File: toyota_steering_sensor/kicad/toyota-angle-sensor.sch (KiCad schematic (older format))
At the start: 32 parts, among them J1 AVR-ISP-6, J2 RJ45, U1 NCP1117-5.0_SOT223, U2 ATMEGA328PB-AU, U3 LS7366R, U4 MCP2515-xSO, U5 AS5047P, U6 TJA1050, Y1 16MHz, Y2 40MHz, Y3 8MHz

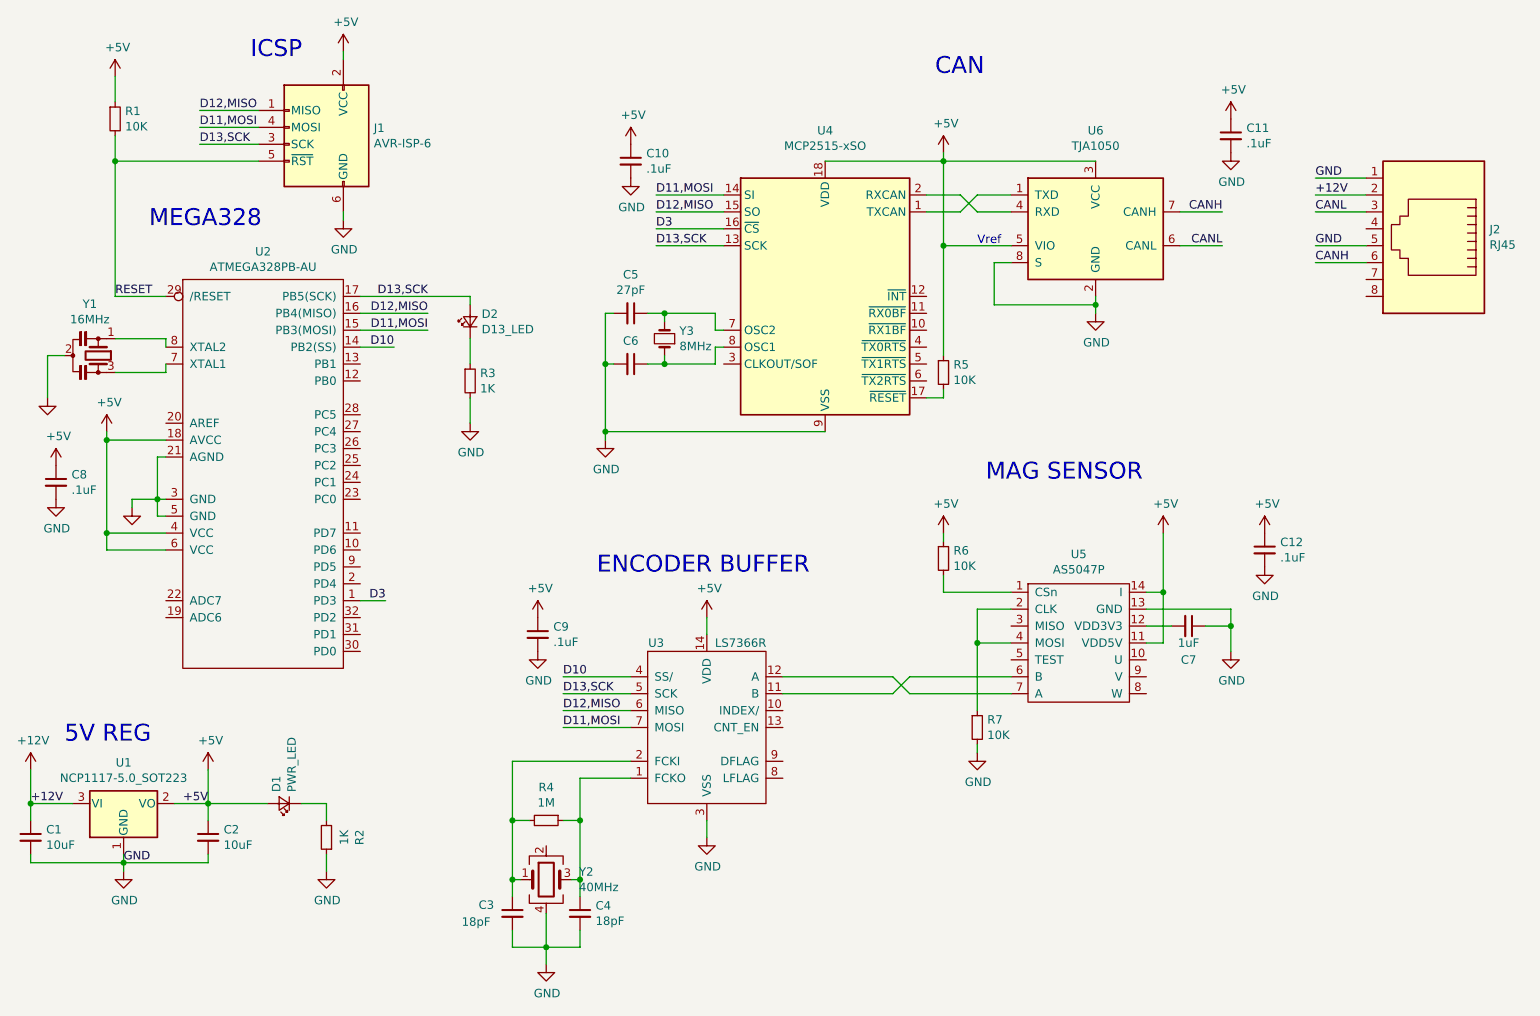
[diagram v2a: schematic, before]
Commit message: add V2 todo outline
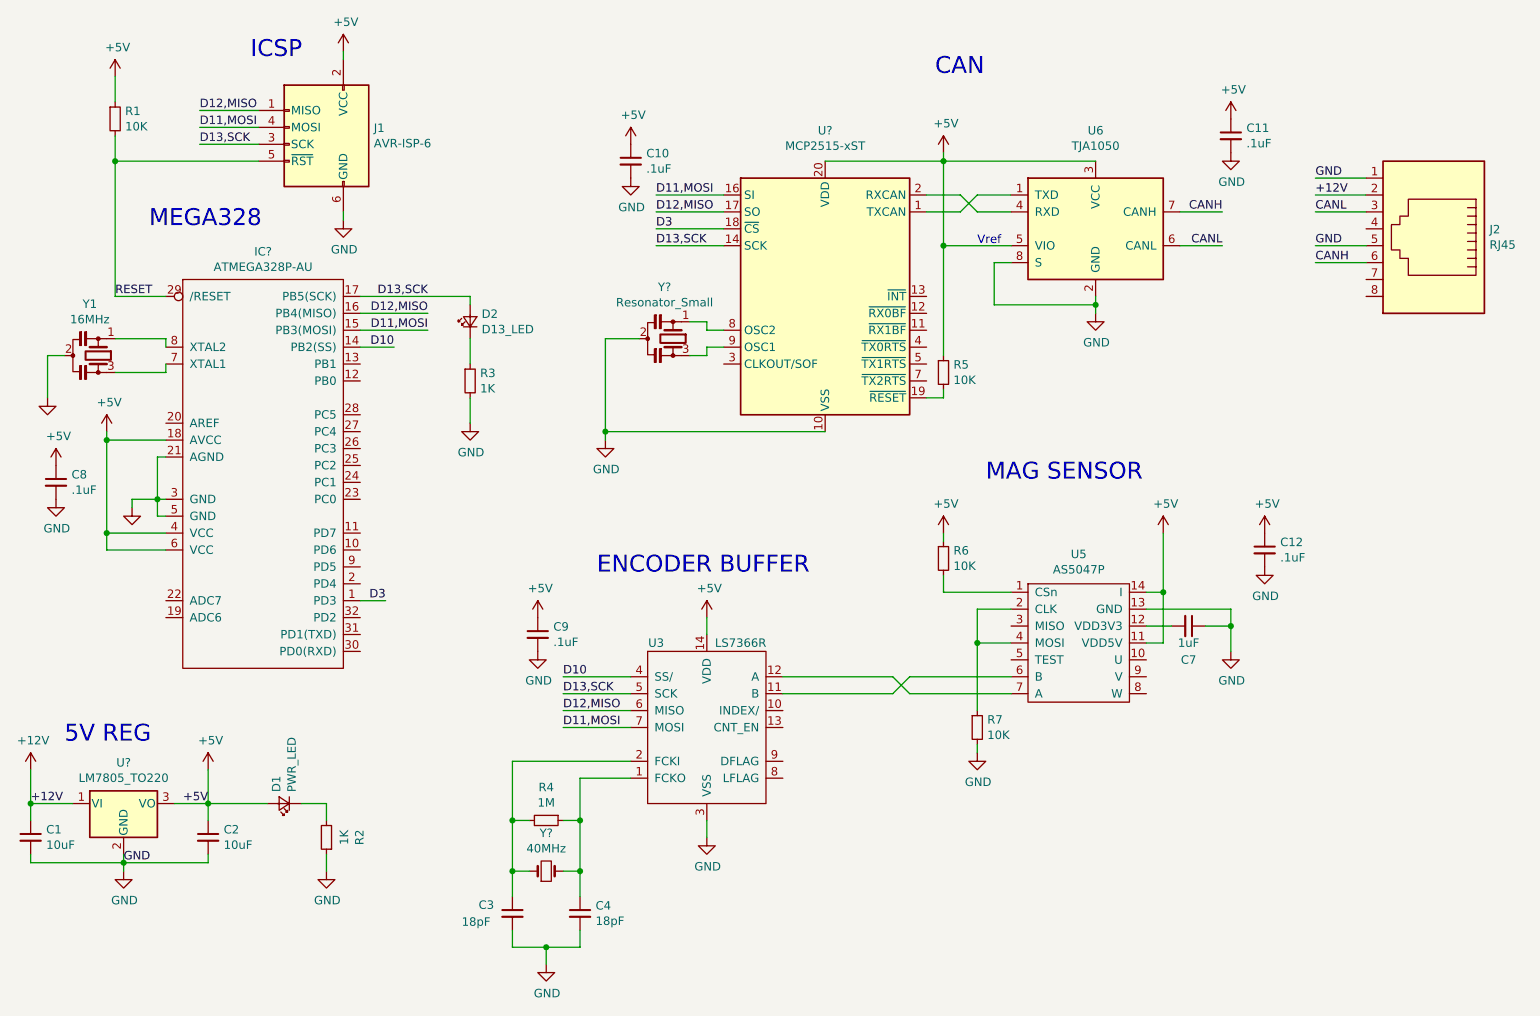
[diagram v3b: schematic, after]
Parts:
- removed C5, C6: 27pF, Capacitor_SMD:C_0603_1608Metric, symbol Device:C_Small
- removed U1: NCP1117-5.0_SOT223, Package_TO_SOT_SMD:SOT-223-3_TabPin2, symbol Regulator_Linear:NCP1117-5.0_SOT223
- removed U2: ATMEGA328PB-AU, Package_QFP:TQFP-32_7x7mm_P0.8mm, symbol Angle_Sensor:ATMEGA328PB-AU
- removed U4: MCP2515-xSO, Package_SO:SOIC-18W_7.5x11.6mm_P1.27mm, symbol Interface_CAN_LIN:MCP2515-xSO
- removed Y2: 40MHz, Crystal:Crystal_SMD_Abracon_ABM8G-4Pin_3.2x2.5mm, symbol Device:Crystal_GND24
- removed Y3: 8MHz, Crystal:Crystal_SMD_Abracon_ABM3-2Pin_5.0x3.2mm_HandSoldering, symbol Device:Crystal_Small
- added IC?: ATMEGA328P-AU, symbol Angle_Sensor:ATMEGA328P-AU
- added U?: MCP2515-xST, Package_SO:TSSOP-20_4.4x6.5mm_P0.65mm, symbol Interface_CAN_LIN:MCP2515-xST
- added U?: LM7805_TO220, Package_TO_SOT_THT:TO-220-3_Vertical, symbol Regulator_Linear:LM7805_TO220
- added Y?: Resonator_Small, symbol Device:Resonator_Small
- added Y?: 40MHz, Crystal:Crystal_SMD_Abracon_ABM3-2Pin_5.0x3.2mm, symbol Device:Crystal_Small
- J2: footprint Connector_RJ:RJ45_Amphenol_54602-x08_Horizontal -> ZSS:Molex 855025008 RJ45
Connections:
- net +12V: now also U?.1 (VI)
- net +5V: now also IC?.18 (AVCC), IC?.4 (VCC), IC?.6 (VCC), U?.20 (VDD), U?.3 (VO)
- net D10: now also IC?.14 (PB2(SS))
- net D11,MOSI: now also IC?.15 (PB3(MOSI)), U?.16 (SI)
- net D12,MISO: now also IC?.16 (PB4(MISO)), U?.17 (SO)
- net D13,SCK: now also IC?.17 (PB5(SCK)), U?.14 (SCK)
- net D3: now also IC?.1 (PD3), U?.18 (~CS)
- net GND: now also IC?.21 (AGND), IC?.3 (GND), IC?.5 (GND), U?.10 (VSS), U?.2 (GND), Y?.2
- net RESET: now also IC?.29 (/RESET)
- net at Y1.3: now also IC?.7 (XTAL1)
- net at Y1.1: now also IC?.8 (XTAL2)
- net at C4.1, R4.1, U3.1 (FCKO): now also Y?.2
- net at C3.1, R4.2, U3.2 (FCKI): now also Y?.1
- net at U6.1 (TXD): now also U?.1 (TXCAN)
- net at R5.2: now also U?.19 (~RESET)
- net at U6.4 (RXD): now also U?.2 (RXCAN)
- new net: U?.8 (OSC2), Y?.1
- new net: U?.9 (OSC1), Y?.3
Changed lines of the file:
@@
 Text Notes 2300 750  0    100  ~ 0
 ICSP
-$Comp
-L Regulator_Linear:NCP1117-5.0_SOT223 U1
-U 1 1 5D46D7B7
-P 1550 5150
-F 0 "U1" H 1550 5392 50  0000 C CNN
-F 1 "NCP1117-5.0_SOT223" H 1550 5301 50  0000 C CNN
-F 2 "Package_TO_SOT_SMD:SOT-223-3_TabPin2" H 1550 5350 50  0001 C CNN
-F 3 "http://www.onsemi.com/pub_link/Collateral/NCP1117-D.PDF" H 1650 4900 50  0001 C CNN
-F 4 "NCP1117ST50T3GOSCT-ND" H 1550 5150 50  0001 C CNN "Digi-Key Part Number"
-	1    1550 5150
-	1    0    0    -1
-$EndComp
 Text Notes 1200 4800 0    100  ~ 0
 5V REG
@@
 Connection ~ 7300 2200
 $Comp
-L Device:Crystal_Small Y3
-U 1 1 5D48BC0B
-P 4750 2400
-F 0 "Y3" V 4796 2312 50  0000 R CNN
-F 1 "8MHz" V 4705 2312 50  0000 R CNN
-F 2 "Crystal:Crystal_SMD_Abracon_ABM3-2Pin_5.0x3.2mm_HandSoldering" H 4750 2400 50  0001 C CNN
-F 3 "~" H 4750 2400 50  0001 C CNN
-F 4 "535-10630-1-ND" H 4750 2400 50  0001 C CNN "Digi-Key Part Number"
-	1    4750 2400
-	0    -1   -1   0
-$EndComp
-$Comp
-L Device:C_Small C5
-U 1 1 5D48BC11
-P 4550 2250
-F 0 "C5" V 4321 2250 50  0000 C CNN
-F 1 "27pF" V 4412 2250 50  0000 C CNN
-F 2 "Capacitor_SMD:C_0603_1608Metric" H 4550 2250 50  0001 C CNN
-F 3 "~" H 4550 2250 50  0001 C CNN
-F 4 "1276-1086-1-ND " H 4550 2250 50  0001 C CNN "Digi-Key Part Number"
-	1    4550 2250
-	0    1    1    0
-$EndComp
-$Comp
-L Device:C_Small C6
-U 1 1 5D48BC17
-P 4550 2550
-F 0 "C6" V 4413 2550 50  0000 C CNN
-F 1 "27pF" V 4412 2550 50  0001 C CNN
-F 2 "Capacitor_SMD:C_0603_1608Metric" H 4550 2550 50  0001 C CNN
-F 3 "~" H 4550 2550 50  0001 C CNN
-F 4 "1276-1086-1-ND " H 4550 2550 50  0001 C CNN "Digi-Key Part Number"
-	1    4550 2550
-	0    1    1    0
-$EndComp
-Wire Wire Line
-	4650 2250 4750 2250
-Wire Wire Line
-	4750 2500 4750 2550
-Wire Wire Line
-	4750 2550 4650 2550
-Wire Wire Line
-	4750 2300 4750 2250
-Wire Wire Line
-	4450 2550 4400 2550
-Wire Wire Line
-	4400 2550 4400 2250
-Wire Wire Line
-	4400 2250 4450 2250
-Wire Wire Line
-	5100 2450 5050 2450
-Wire Wire Line
-	5050 2450 5050 2550
-Wire Wire Line
-	5050 2550 4750 2550
-Connection ~ 4750 2550
-Wire Wire Line
-	5100 2350 5050 2350
-Wire Wire Line
-	5050 2350 5050 2250
-Wire Wire Line
-	5050 2250 4750 2250
-Connection ~ 4750 2250
-$Comp
 L power:GND #PWR013
 U 1 1 5D49BBE0
@@
 	1    0    0    -1
 $EndComp
-Connection ~ 4400 2550
 $Comp
 L Device:R_Small R5
@@
 Text Label 1550 5500 0    50   ~ 0
 GND
-Connection ~ 4400 2950
-Wire Wire Line
-	4400 2950 4400 2550
 Wire Wire Line
 	4400 3000 4400 2950
@@
 Wire Wire Line
 	5700 2950 4400 2950
-$Comp
-L Interface_CAN_LIN:MCP2515-xSO U4
-U 1 1 5D479C62
-P 5700 2150
-F 0 "U4" H 5700 3131 50  0000 C CNN
-F 1 "MCP2515-xSO" H 5700 3040 50  0000 C CNN
-F 2 "Package_SO:SOIC-18W_7.5x11.6mm_P1.27mm" H 5700 1250 50  0001 C CIN
-F 3 "http://ww1.microchip.com/downloads/en/DeviceDoc/21801e.pdf" H 5800 1350 50  0001 C CNN
-F 4 "MCP2515T-I/SOCT-ND" H 5700 2150 50  0001 C CNN "Digi-Key Part Number"
-	1    5700 2150
-	1    0    0    -1
-$EndComp
 Wire Wire Line
 	6800 4400 6200 4400
@@
 F 0 "J2" H 8970 1754 50  0000 R CNN
 F 1 "RJ45" H 8970 1845 50  0000 R CNN
-F 2 "Connector_RJ:RJ45_Amphenol_54602-x08_Horizontal" V 9300 1775 50  0001 C CNN
+F 2 "ZSS:Molex 855025008 RJ45" V 9300 1775 50  0001 C CNN
 F 3 "~" V 9300 1775 50  0001 C CNN
 F 4 "609-1046-ND" H 9300 1750 50  0001 C CNN "Digi-Key Part Number"
@@
 	0    1    1    0
 $EndComp
-$Comp
-L Angle_Sensor:ATMEGA328PB-AU U2
-U 1 1 5D43444B
-P 2400 1950
-F 0 "U2" H 2375 2015 50  0000 C CNN
-F 1 "ATMEGA328PB-AU" H 2375 1924 50  0000 C CNN
-F 2 "Package_QFP:TQFP-32_7x7mm_P0.8mm" H 2400 -500 50  0001 C CNN
-F 3 "" H 2400 -500 50  0001 C CNN
-F 4 "ATMEGA328PB-AU-ND" H 2400 1950 50  0001 C CNN "Digi-Key Part Number"
-	1    2400 1950
-	1    0    0    -1
-$EndComp
 Wire Wire Line
 	1800 2450 1800 2400
@@
 	1    0    0    -1
 $EndComp
-Wire Wire Line
-	4250 5250 4250 5600
-Wire Wire Line
-	3850 5250 3850 5600
-$Comp
-L Device:Crystal_GND24 Y2
-U 1 1 5D5A4D2A
-P 4050 5600
-F 0 "Y2" H 4244 5646 50  0000 L CNN
-F 1 "40MHz" H 4244 5555 50  0000 L CNN
-F 2 "Crystal:Crystal_SMD_Abracon_ABM8G-4Pin_3.2x2.5mm" H 4050 5600 50  0001 C CNN
-F 3 "~" H 4050 5600 50  0001 C CNN
-F 4 "535-13401-1-ND" H 4050 5600 50  0001 C CNN "Digi-Key Part Number"
-	1    4050 5600
-	1    0    0    -1
-$EndComp
-Wire Wire Line
-	4250 5600 4200 5600
-Connection ~ 4250 5600
-Wire Wire Line
-	4250 5600 4250 5700
-Wire Wire Line
-	3900 5600 3850 5600
-Connection ~ 3850 5600
-Wire Wire Line
-	3850 5600 3850 5700
-Wire Wire Line
-	4050 5800 4050 6000
 $Comp
 L power:GND #PWR0111
@@
 	1    0    0    -1
 $EndComp
+$Comp
+L Interface_CAN_LIN:MCP2515-xST U?
+U 1 1 5D717111
+P 5700 2150
+F 0 "U?" H 5700 3131 50  0000 C CNN
+F 1 "MCP2515-xST" H 5700 3040 50  0000 C CNN
+F 2 "Package_SO:TSSOP-20_4.4x6.5mm_P0.65mm" H 5700 1250 50  0001 C CIN
+F 3 "http://ww1.microchip.com/downloads/en/DeviceDoc/21801e.pdf" H 5800 1350 50  0001 C CNN
+	1    5700 2150
+	1    0    0    -1
+$EndComp
+$Comp
+L Device:Resonator_Small Y?
+U 1 1 5D72675F
+P 4800 2400
+F 0 "Y?" V 4495 2350 50  0000 C CNN
+F 1 "Resonator_Small" V 4586 2350 50  0000 C CNN
+F 2 "" H 4775 2400 50  0001 C CNN
+F 3 "~" H 4775 2400 50  0001 C CNN
+	1    4800 2400
+	0    1    1    0
+$EndComp
+Wire Wire Line
+	5100 2350 5000 2350
+Wire Wire Line
+	5000 2350 5000 2300
+Wire Wire Line
+	5000 2300 4900 2300
+Wire Wire Line
+	5100 2450 5000 2450
+Wire Wire Line
+	5000 2450 5000 2500
+Wire Wire Line
+	5000 2500 4900 2500
+Wire Wire Line
+	4600 2400 4400 2400
+Wire Wire Line
+	4400 2400 4400 2950
+Connection ~ 4400 2950
+Wire Wire Line
+	4250 5250 4250 5550
+Wire Wire Line
+	3850 5250 3850 5550
+$Comp
+L Device:Crystal_Small Y?
+U 1 1 5D73B9B9
+P 4050 5550
+F 0 "Y?" H 4050 5775 50  0000 C CNN
+F 1 "40MHz" H 4050 5684 50  0000 C CNN
+F 2 "Crystal:Crystal_SMD_Abracon_ABM3-2Pin_5.0x3.2mm" H 4050 5550 50  0001 C CNN
+F 3 "~" H 4050 5550 50  0001 C CNN
+	1    4050 5550
+	1    0    0    -1
+$EndComp
+Wire Wire Line
+	4150 5550 4250 5550
+Connection ~ 4250 5550
+Wire Wire Line
+	4250 5550 4250 5700
+Wire Wire Line
+	3950 5550 3850 5550
+Connection ~ 3850 5550
+Wire Wire Line
+	3850 5550 3850 5700
+$Comp
+L Angle_Sensor:ATMEGA328P-AU IC?
+U 1 1 5D74BDEC
+P 2400 1950
+F 0 "IC?" H 2375 2015 50  0000 C CNN
+F 1 "ATMEGA328P-AU" H 2375 1924 50  0000 C CNN
+F 2 "" H 2400 -500 50  0001 C CNN
+F 3 "" H 2400 -500 50  0001 C CNN
+	1    2400 1950
+	1    0    0    -1
+$EndComp
+$Comp
+L Regulator_Linear:LM7805_TO220 U?
+U 1 1 5D74D832
+P 1550 5150
+F 0 "U?" H 1550 5392 50  0000 C CNN
+F 1 "LM7805_TO220" H 1550 5301 50  0000 C CNN
+F 2 "Package_TO_SOT_THT:TO-220-3_Vertical" H 1550 5375 50  0001 C CIN
+F 3 "http://www.fairchildsemi.com/ds/LM/LM7805.pdf" H 1550 5100 50  0001 C CNN
+	1    1550 5150
+	1    0    0    -1
+$EndComp
